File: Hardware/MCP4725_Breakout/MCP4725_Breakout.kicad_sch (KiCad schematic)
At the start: 16 parts, among them U1 MCP4725

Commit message: Saves progress
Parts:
- removed C1: 0.1uF, MCP4725_Breakout:0603-CAP, symbol MCP4725_Breakout-eagle-import:CAP0603-CAP
- removed FID1, FID2: FIDUCIAL1X2, MCP4725_Breakout:FIDUCIAL-1X2, symbol MCP4725_Breakout-eagle-import:FIDUCIAL1X2
- removed FRAME2: FRAME-LETTER, MCP4725_Breakout:CREATIVE_COMMONS, symbol MCP4725_Breakout-eagle-import:FRAME-LETTER
- removed GND0: LOGO-SFESK, MCP4725_Breakout:SFE-LOGO-FLAME, symbol MCP4725_Breakout-eagle-import:LOGO-SFESK
- removed JP5: M04PTH, MCP4725_Breakout:1X04, symbol MCP4725_Breakout-eagle-import:M04PTH
- removed JP6: M02PTH, MCP4725_Breakout:1X02, symbol MCP4725_Breakout-eagle-import:M02PTH
- removed LOGO1: OSHW-LOGOS, MCP4725_Breakout:OSHW-LOGO-S, symbol MCP4725_Breakout-eagle-import:OSHW-LOGOS
- removed STANDOFF1, STANDOFF2: STAND-OFF, MCP4725_Breakout:STAND-OFF, symbol MCP4725_Breakout-eagle-import:STAND-OFF
- removed U1: MCP4725, MCP4725_Breakout:SOT23-6, symbol MCP4725_Breakout-eagle-import:MCP4725SOT-23
- added C1: 0.1uF, SparkFun-Capacitor:C_0603_1608Metric, symbol SparkFun-Capacitor:0.1uF_0603_25V_20%
- added FID1, FID2, FID3, FID4: Fiducial_0.5mm, SparkFun-Aesthetic:Fiducial_0.5mm_Mask1mm, symbol SparkFun-Aesthetic:Fiducial_0.5mm
- added G1: OSHW_Logo, SparkFun-Aesthetic:Creative_Commons_License, symbol SparkFun-Aesthetic:OSHW_Logo
- added G2: SparkFun_Logo, symbol SparkFun-Aesthetic:SparkFun_Logo
- added J1: Conn_01x02, SparkFun-Connector:1x02_P2.54mm, symbol SparkFun-Connector:Conn_01x02_P2.54mm
- added J2: I2C, SparkFun-Connector:1x04_P2.54mm, symbol SparkFun-Connector:I2CStandard_1x04_P2.54mm
- added ST1, ST2: Standoff, SparkFun-Hardware:Standoff, symbol SparkFun-Hardware:Standoff
- added U2: MCP4725, SparkFun-Semiconductor-Standard:SOT23-6, symbol SparkFun-IC-Amplifier:MCP4725
- JP1: value ~ -> I2C
- JP2: value ~ -> ADDR
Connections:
- net 3.3V: now also C1.1, J2.2 (Pin_2), U2.3 (VDD)
- net GND: now also C1.2, J1.2 (Pin_2), J2.1 (Pin_1), U2.2 (VSS)
- net SCL: now also R5.1, J2.4 (Pin_4), U2.4 (SDA); no longer R4.1
- net SDA: now also R4.1, J2.3 (Pin_3), U2.5 (SCL); no longer R5.1
- net ADDR: now reaches JP2.2 (B)
- net ADDR: now also U2.6 (AO)
- new net VOUT: J1.1 (Pin_1), U2.1 (VOUT)
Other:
- note added: "Address Jumper"
- note added: "Connectors"
- note added: "Cut jumper to disable I2C pull-ups."
- note added: "Default Address: 0x60"
- note added: "I2C DAC - MCP4725"
- note added: "I2C Jumper"
- note added: "VDD: 2.7V - 5.5V"
- note removed: "14"
- note removed: "I2C Address GND = 1100000 (0x60) (Default) VCC - 1100001 (0x61)"
- note removed: "Joel Bartlett"
- note removed: "Vcc = 2.7V to 5.5V"
- company: (none) -> SparkFun Electronics
- title: (none) -> SparkFun I2C DAC - MCP4725
- moved on the sheet: JP1, JP2, R1, R4, R5

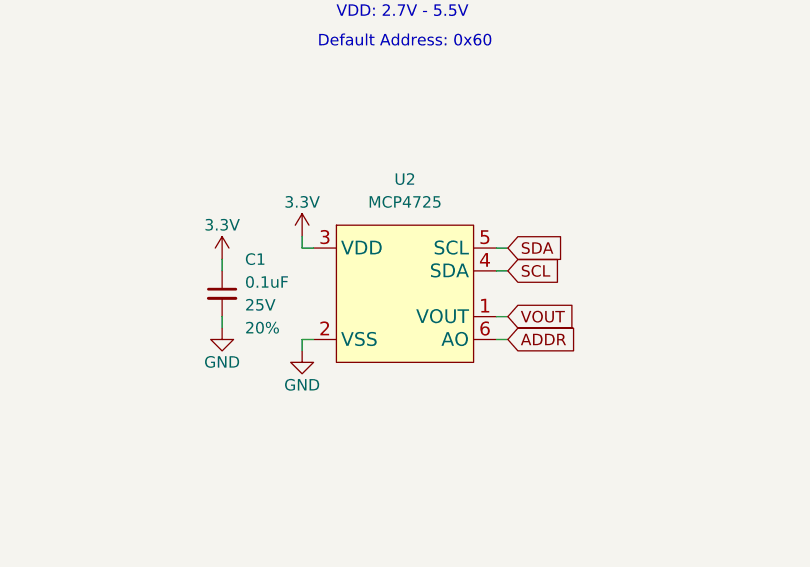
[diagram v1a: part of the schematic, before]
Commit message: Fixes DAC symbol, aligns Qwiic connector, removes extra pour
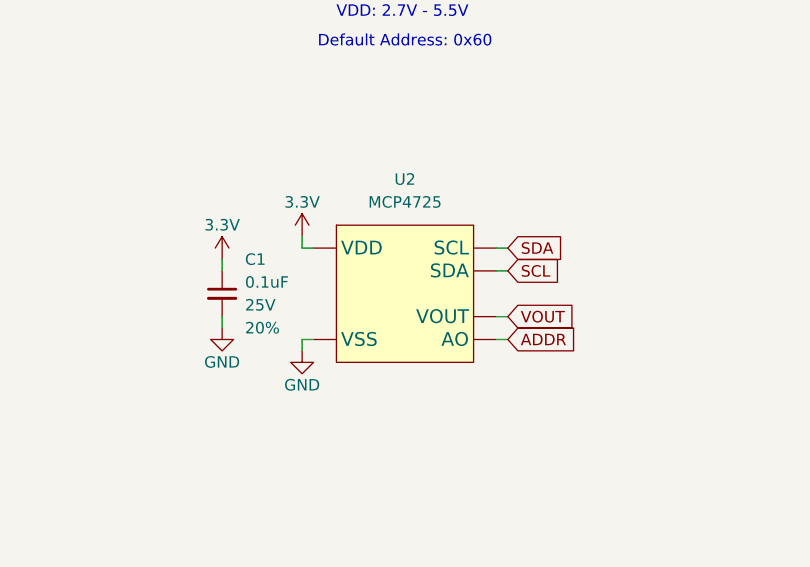
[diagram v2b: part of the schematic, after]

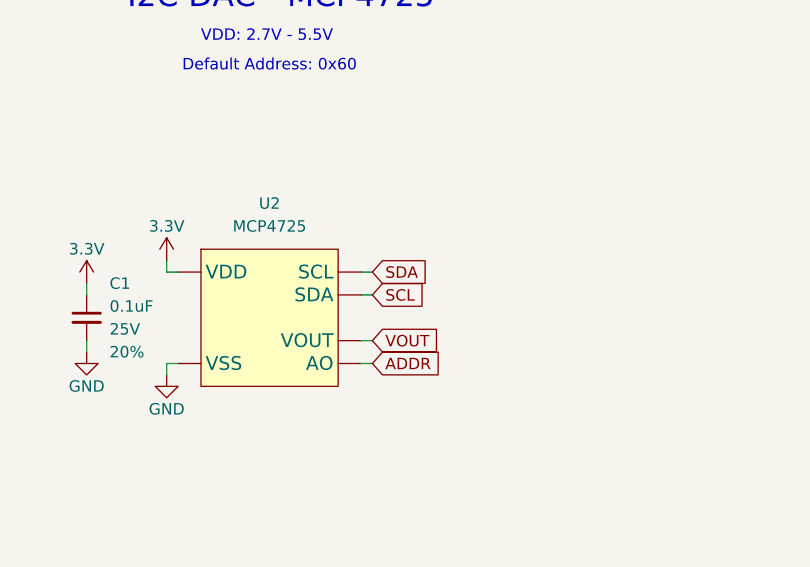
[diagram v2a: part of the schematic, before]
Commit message: Fixes swapped pins on SCL/SDA
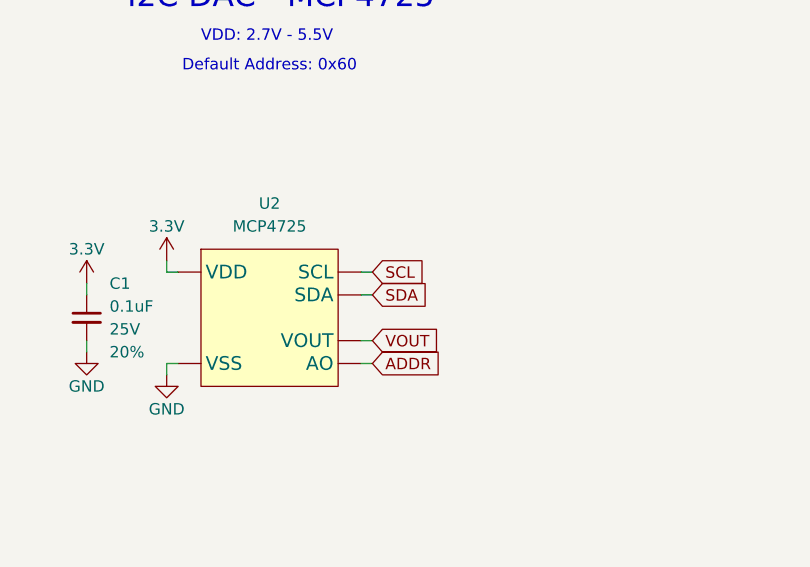
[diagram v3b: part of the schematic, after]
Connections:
- net SCL: now also U2.5 (SCL); no longer U2.4 (SDA)
- net SDA: now also U2.4 (SDA); no longer U2.5 (SCL)
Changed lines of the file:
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@@
+	(wire
+		(pts
+			(xy 96.52 54.61) (xy 97.79 54.61)
+		)
+		(stroke
+			(width 0)
+			(type default)
+		)
+	)
 	(wire
 		(pts
@@
 	(wire
 		(pts
+			(xy 66.04 53.34) (xy 66.04 54.61)
+		)
+		(stroke
+			(width 0.1524)
+			(type solid)
+		)
+	)
+	(wire
+		(pts
+			(xy 49.53 149.86) (xy 50.8 149.86)
+		)
+		(stroke
+			(width 0.1524)
+			(type solid)
+		)
+	)
+	(wire
+		(pts
+			(xy 50.8 149.86) (xy 50.8 147.32)
+		)
+		(stroke
+			(width 0.1524)
+			(type solid)
+		)
+	)
+	(wire
+		(pts
+			(xy 223.52 64.77) (xy 223.52 63.5)
+		)
+		(stroke
+			(width 0.1524)
+			(type solid)
+		)
+	)
+	(wire
+		(pts
+			(xy 139.7 129.54) (xy 139.7 128.27)
+		)
+		(stroke
+			(width 0.1524)
+			(type solid)
+		)
+	)
+	(wire
+		(pts
+			(xy 222.25 52.07) (xy 224.79 52.07)
+		)
+		(stroke
+			(width 0.1524)
+			(type solid)
+		)
+	)
+	(polyline
+		(pts
+			(xy 12.7 91.44) (xy 284.48 91.44)
+		)
+		(stroke
+			(width 0)
+			(type dash)
+		)
+	)
+	(wire
+		(pts
+			(xy 96.52 59.69) (xy 97.79 59.69)
+		)
+		(stroke
+			(width 0)
+			(type default)
+		)
+	)
+	(polyline
+		(pts
+			(xy 160.02 11.43) (xy 160.02 91.44)
+		)
+		(stroke
+			(width 0)
+			(type dash)
+		)
+	)
+	(wire
+		(pts
+			(xy 223.52 49.53) (xy 223.52 63.5)
+		)
+		(stroke
+			(width 0.1524)
+			(type solid)
+		)
+	)
+	(wire
+		(pts
+			(xy 139.7 142.24) (xy 139.7 140.97)
+		)
+		(stroke
+			(width 0.1524)
+			(type solid)
+		)
+	)
+	(wire
+		(pts
+			(xy 50.8 139.7) (xy 52.07 139.7)
+		)
+		(stroke
+			(width 0.1524)
+			(type solid)
+		)
+	)
+	(wire
+		(pts
+			(xy 224.79 46.99) (xy 224.79 52.07)
+		)
+		(stroke
+			(width 0)
+			(type default)
+		)
+	)
+	(wire
+		(pts
+			(xy 74.93 52.07) (xy 74.93 50.8)
+		)
+		(stroke
+			(width 0.1524)
+			(type solid)
+		)
+	)
+	(wire
+		(pts
+			(xy 96.52 62.23) (xy 97.79 62.23)
+		)
+		(stroke
+			(width 0)
+			(type default)
+		)
+	)
+	(wire
+		(pts
+			(xy 74.93 62.23) (xy 74.93 63.5)
+		)
+		(stroke
+			(width 0)
+			(type default)
+		)
+	)
+	(wire
+		(pts
+			(xy 66.04 59.69) (xy 66.04 60.96)
+		)
+		(stroke
+			(width 0.1524)
+			(type solid)
+		)
+	)
+	(wire
+		(pts
 			(xy 96.52 52.07) (xy 97.79 52.07)
 		)
@@
 			(width 0)
 			(type default)
-		)
-	)
-	(wire
-		(pts
-			(xy 66.04 53.34) (xy 66.04 54.61)
-		)
-		(stroke
-			(width 0.1524)
-			(type solid)
-		)
-	)
-	(wire
-		(pts
-			(xy 49.53 149.86) (xy 50.8 149.86)
-		)
-		(stroke
-			(width 0.1524)
-			(type solid)
-		)
-	)
-	(wire
-		(pts
-			(xy 50.8 149.86) (xy 50.8 147.32)
-		)
-		(stroke
-			(width 0.1524)
-			(type solid)
-		)
-	)
-	(wire
-		(pts
-			(xy 223.52 64.77) (xy 223.52 63.5)
-		)
-		(stroke
-			(width 0.1524)
-			(type solid)
-		)
-	)
-	(wire
-		(pts
-			(xy 139.7 129.54) (xy 139.7 128.27)
-		)
-		(stroke
-			(width 0.1524)
-			(type solid)
-		)
-	)
-	(wire
-		(pts
-			(xy 222.25 52.07) (xy 224.79 52.07)
-		)
-		(stroke
-			(width 0.1524)
-			(type solid)
-		)
-	)
-	(polyline
-		(pts
-			(xy 12.7 91.44) (xy 284.48 91.44)
-		)
-		(stroke
-			(width 0)
-			(type dash)
-		)
-	)
-	(wire
-		(pts
-			(xy 96.52 59.69) (xy 97.79 59.69)
-		)
-		(stroke
-			(width 0)
-			(type default)
-		)
-	)
-	(polyline
-		(pts
-			(xy 160.02 11.43) (xy 160.02 91.44)
-		)
-		(stroke
-			(width 0)
-			(type dash)
-		)
-	)
-	(wire
-		(pts
-			(xy 223.52 49.53) (xy 223.52 63.5)
-		)
-		(stroke
-			(width 0.1524)
-			(type solid)
-		)
-	)
-	(wire
-		(pts
-			(xy 96.52 54.61) (xy 97.79 54.61)
-		)
-		(stroke
-			(width 0)
-			(type default)
-		)
-	)
-	(wire
-		(pts
-			(xy 139.7 142.24) (xy 139.7 140.97)
-		)
-		(stroke
-			(width 0.1524)
-			(type solid)
-		)
-	)
-	(wire
-		(pts
-			(xy 50.8 139.7) (xy 52.07 139.7)
-		)
-		(stroke
-			(width 0.1524)
-			(type solid)
-		)
-	)
-	(wire
-		(pts
-			(xy 224.79 46.99) (xy 224.79 52.07)
-		)
-		(stroke
-			(width 0)
-			(type default)
-		)
-	)
-	(wire
-		(pts
-			(xy 74.93 52.07) (xy 74.93 50.8)
-		)
-		(stroke
-			(width 0.1524)
-			(type solid)
-		)
-	)
-	(wire
-		(pts
-			(xy 96.52 62.23) (xy 97.79 62.23)
-		)
-		(stroke
-			(width 0)
-			(type default)
-		)
-	)
-	(wire
-		(pts
-			(xy 74.93 62.23) (xy 74.93 63.5)
-		)
-		(stroke
-			(width 0)
-			(type default)
-		)
-	)
-	(wire
-		(pts
-			(xy 66.04 59.69) (xy 66.04 60.96)
-		)
-		(stroke
-			(width 0.1524)
-			(type solid)
 		)
 	)
@@
 		)
 	)
-	(global_label "SCL"
-		(shape input)
-		(at 97.79 54.61 0)
-		(fields_autoplaced yes)
-		(effects
-			(font
-				(size 1.27 1.27)
-			)
-			(justify left)
-		)
-		(property "Intersheetrefs" "${INTERSHEET_REFS}"
-			(at 104.2828 54.61 0)
-			(effects
-				(font
-					(size 1.27 1.27)
-				)
-				(justify left)
-				(hide yes)
-			)
-		)
-	)
 	(global_label "SDA"
 		(shape input)
@@
 	(global_label "SCL"
 		(shape input)
+		(at 97.79 52.07 0)
+		(fields_autoplaced yes)
+		(effects
+			(font
+				(size 1.27 1.27)
+			)
+			(justify left)
+		)
+		(property "Intersheetrefs" "${INTERSHEET_REFS}"
+			(at 104.2828 52.07 0)
+			(effects
+				(font
+					(size 1.27 1.27)
+				)
+				(justify left)
+				(hide yes)
+			)
+		)
+	)
+	(global_label "SDA"
+		(shape input)
+		(at 97.79 54.61 0)
+		(fields_autoplaced yes)
+		(effects
+			(font
+				(size 1.27 1.27)
+			)
+			(justify left)
+		)
+		(property "Intersheetrefs" "${INTERSHEET_REFS}"
+			(at 104.3433 54.61 0)
+			(effects
+				(font
+					(size 1.27 1.27)
+				)
+				(justify left)
+				(hide yes)
+			)
+		)
+	)
+	(global_label "SCL"
+		(shape input)
 		(at 59.69 149.86 0)
 		(fields_autoplaced yes)
@@
 			(effects
 				(font
-					(size 1.27 1.27)
-				)
-				(justify left)
-				(hide yes)
-			)
-		)
-	)
-	(global_label "SDA"
-		(shape input)
-		(at 97.79 52.07 0)
-		(fields_autoplaced yes)
-		(effects
-			(font
-				(size 1.27 1.27)
-			)
-			(justify left)
-		)
-		(property "Intersheetrefs" "${INTERSHEET_REFS}"
-			(at 104.3433 52.07 0)
-			(effects
-				(font

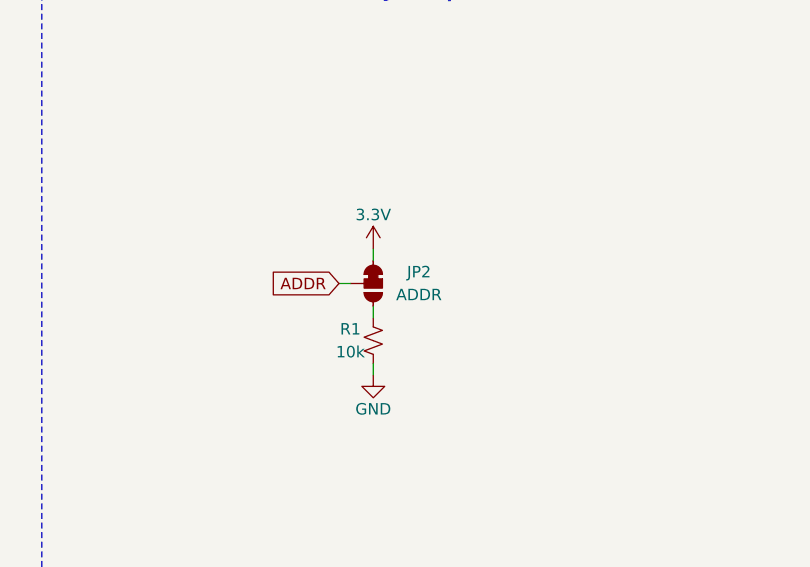
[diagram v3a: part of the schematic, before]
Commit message: Adds Qwiic Logo, power LED, adds "DAC" to product silk
* Fixes the address jumper
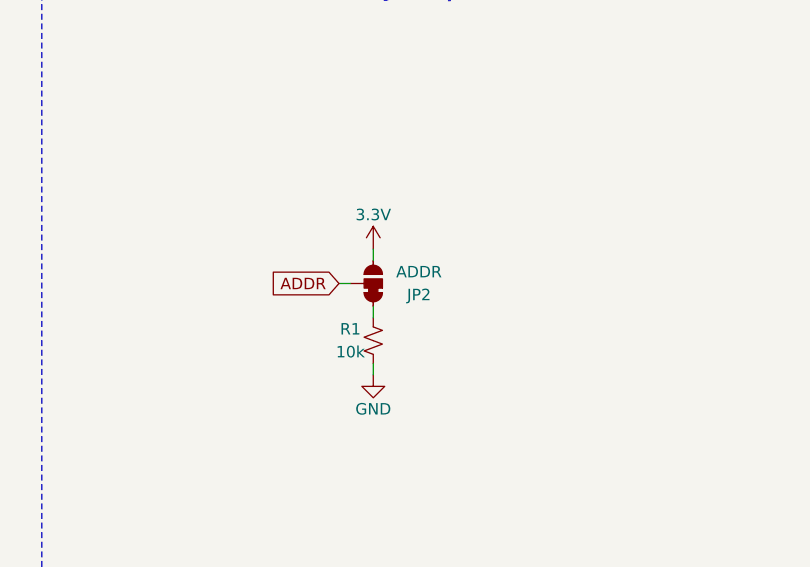
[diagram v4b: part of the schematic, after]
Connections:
- net 3.3V: now also JP2.3 (C); no longer JP2.1 (A)
- net at R1.2: now also JP2.1 (A); no longer JP2.3 (C)
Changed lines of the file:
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@@
 		(title "SparkFun I2C DAC - MCP4725")
 		(date "2026-03-13")
-		(rev "v10")
+		(rev "v20")
 		(company "SparkFun Electronics")
 		(comment 1 "Designed By: Joel Bartlett")
@@
 	(wire
 		(pts
+			(xy 135.89 132.08) (xy 137.16 132.08)
+		)
+		(stroke
+			(width 0)
+			(type default)
+		)
+	)
+	(wire
+		(pts
 			(xy 58.42 149.86) (xy 59.69 149.86)
 		)
@@
 	(wire
 		(pts
-			(xy 139.7 135.89) (xy 139.7 134.62)
-		)
-		(stroke
-			(width 0.1524)
-			(type solid)
-		)
-	)
-	(wire
-		(pts
-			(xy 135.89 132.08) (xy 137.16 132.08)
-		)
-		(stroke
-			(width 0.1524)
-			(type solid)
-		)
-	)
-	(wire
-		(pts
 			(xy 50.8 139.7) (xy 50.8 142.24)
 		)
@@
 	(wire
 		(pts
-			(xy 139.7 129.54) (xy 139.7 128.27)
-		)
-		(stroke
-			(width 0.1524)
-			(type solid)
-		)
-	)
-	(wire
-		(pts
 			(xy 222.25 52.07) (xy 224.79 52.07)
 		)
@@
 	(wire
 		(pts
+			(xy 139.7 134.62) (xy 139.7 135.89)
+		)
+		(stroke
+			(width 0)
+			(type default)
+		)
+	)
+	(wire
+		(pts
 			(xy 224.79 46.99) (xy 224.79 52.07)
 		)
@@
 		(pts
 			(xy 96.52 52.07) (xy 97.79 52.07)
+		)
+		(stroke
+			(width 0)
+			(type default)
+		)
+	)
+	(wire
+		(pts
+			(xy 139.7 128.27) (xy 139.7 129.54)
 		)
 		(stroke
@@
 		(lib_id "SparkFun-Jumper:SolderJumper_3_Bridged12")
 		(at 139.7 132.08 270)
+		(mirror x)
 		(unit 1)
 		(exclude_from_sim no)
@@
 		(dnp no)
 		(property "Reference" "JP2"
+			(at 144.78 133.35 90)
+			(effects
+				(font
+					(size 1.27 1.27)
+				)
+			)
+		)
+		(property "Value" "ADDR"
 			(at 144.78 130.81 90)
 			(effects
 				(font
-					(size 1.27 1.27)
-				)
-			)
-		)
-		(property "Value" "ADDR"
-			(at 144.78 133.35 90)
-			(effects
-				(font
